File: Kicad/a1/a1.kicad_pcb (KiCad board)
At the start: 2 copper layers, 190 x 100 mm, 119 parts, among them J1 Conn_02x03_Odd_Even, J2 VGA, J3 AudioJack4, J4 Conn_02x17_Odd_Even, J6 Barrel Jack, J7 DE9_Plug, J8 DE9_Plug, SW1 Q, SW10 P, SW11 A, SW12 S, SW13 D, SW14 F, SW15 G, SW16 H, SW17 J, SW18 K, SW19 L, SW2 W, SW20 ENT, SW21 Z, SW22 X, SW23 C, SW24 V, SW25 SHIFT, SW26 ALT, SW27 B, SW28 N, SW29 M, SW3 E, SW30 SPACE, SW31 SW_Push, SW32 SW_SPDT, SW4 R, SW5 T, SW6 Y, SW7 U, SW8 I, SW9 O, U1 74HC590A, U10 74HC32, U11 74HC174, U12 74HC4520, U2 74HC590A, U3 62256, U4 SST39SF0x0, U5 W65C02SxP, U6 74HCT541, U7 74HC166, U8 74HC14, U9 74HC10, Y1 16Mhz

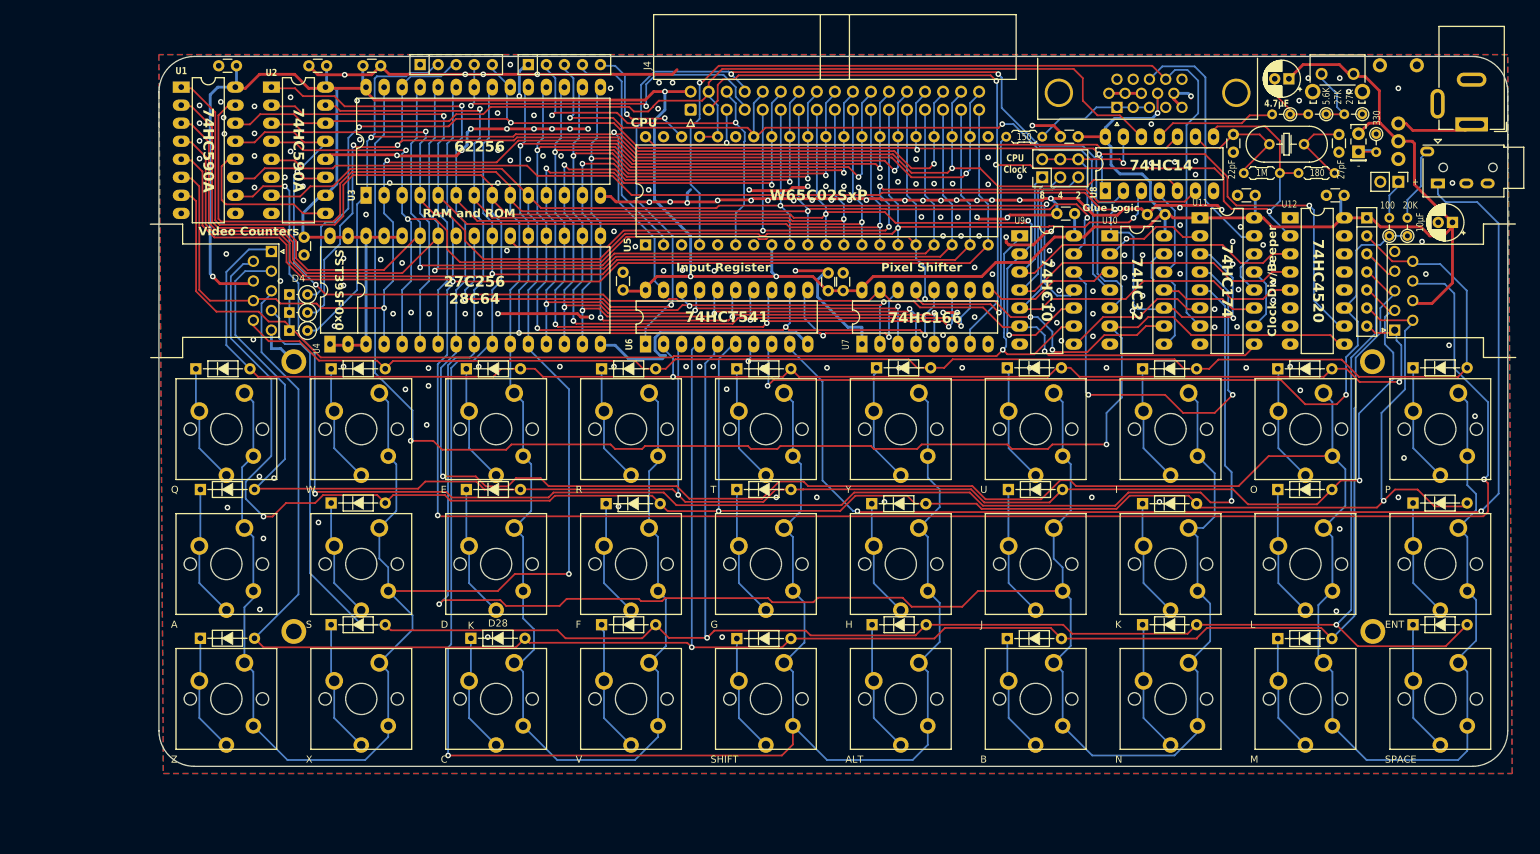
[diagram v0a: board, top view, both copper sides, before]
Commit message: tweak pcb, change key layout
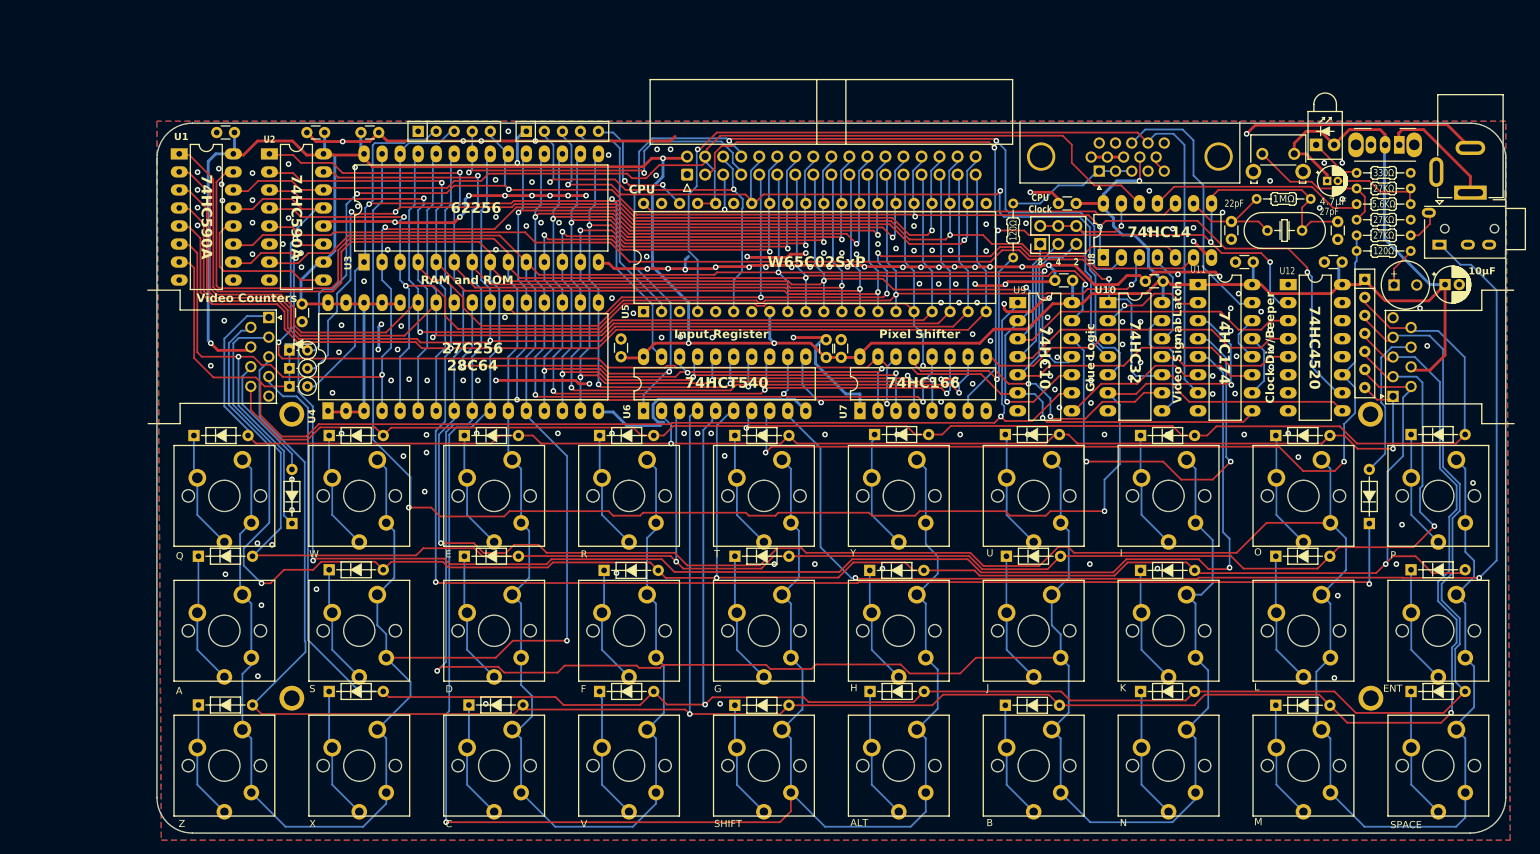
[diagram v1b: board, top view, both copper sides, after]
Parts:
- removed D1: LED, LED_THT:LED_Rectangular_W5.0mm_H2.0mm
- removed R11: 5.6K, PCM_Resistor_THT_US_AKL:R_Axial_DIN0204_L3.6mm_D1.6mm_P2.54mm_Vertical
- removed R12, R13: 27K, PCM_Resistor_THT_US_AKL:R_Axial_DIN0204_L3.6mm_D1.6mm_P2.54mm_Vertical
- removed R14: 20K, PCM_Resistor_THT_US_AKL:R_Axial_DIN0204_L3.6mm_D1.6mm_P2.54mm_Vertical
- added D37: LED, PCM_LED_THT_AKL:LED_Indicator_D3.0mm_W4.6mm_L6.5mm, F.Cu at (218.3, 43.1)
- added D5: 1N4148, PCM_Diode_THT_AKL_Double:D_DO-35_SOD27_P7.62mm_Horizontal, F.Cu at (225.8, 96.4)
- added D6: 1N4148, PCM_Diode_THT_AKL_Double:D_DO-35_SOD27_P7.62mm_Horizontal, F.Cu at (74.0, 96.4)
- added R6: 27KΩ, PCM_Resistor_THT_AKL_Double:R_Axial_DIN0204_L3.6mm_D1.6mm_P7.62mm_Horizontal, F.Cu at (224.0, 55.8)
- added R7: 120Ω, PCM_Resistor_THT_AKL_Double:R_Axial_DIN0204_L3.6mm_D1.6mm_P7.62mm_Horizontal, F.Cu at (175.6, 58.9)
- added R8: 120Ω, PCM_Resistor_THT_AKL_Double:R_Axial_DIN0204_L3.6mm_D1.6mm_P7.62mm_Horizontal, F.Cu at (224.0, 58.0)
- BZ1: footprint Connector_PinHeader_2.54mm:PinHeader_1x02_P2.54mm_Vertical -> Buzzer_Beeper:MagneticBuzzer_Kingstate_KCG0601
- C3: footprint PCM_Capacitor_THT_AKL:CP_Radial_D5.0mm_P2.00mm -> PCM_Capacitor_THT_AKL:CP_Radial_D4.0mm_P1.50mm
- R1: value 1M -> 330Ω; footprint PCM_Resistor_THT_AKL_Double:R_Axial_DIN0204_L3.6mm_D1.6mm_P5.08mm_Horizontal -> PCM_Resistor_THT_AKL_Double:R_Axial_DIN0204_L3.6mm_D1.6mm_P7.62mm_Horizontal
- R2: value 180 -> 1MΩ; footprint PCM_Resistor_THT_AKL_Double:R_Axial_DIN0204_L3.6mm_D1.6mm_P5.08mm_Horizontal -> PCM_Resistor_THT_AKL_Double:R_Axial_DIN0204_L3.6mm_D1.6mm_P7.62mm_Horizontal
- R3: value 150 -> 27KΩ; footprint PCM_Resistor_THT_AKL_Double:R_Axial_DIN0204_L3.6mm_D1.6mm_P5.08mm_Horizontal -> PCM_Resistor_THT_AKL_Double:R_Axial_DIN0204_L3.6mm_D1.6mm_P7.62mm_Horizontal
- R4: value 330 -> 27KΩ; footprint PCM_Resistor_THT_US_AKL:R_Axial_DIN0204_L3.6mm_D1.6mm_P2.54mm_Vertical -> PCM_Resistor_THT_AKL_Double:R_Axial_DIN0204_L3.6mm_D1.6mm_P7.62mm_Horizontal
- R5: value 100 -> 5.6KΩ; footprint PCM_Resistor_THT_US_AKL:R_Axial_DIN0204_L3.6mm_D1.6mm_P2.54mm_Vertical -> PCM_Resistor_THT_AKL_Double:R_Axial_DIN0204_L3.6mm_D1.6mm_P7.62mm_Horizontal
- U6: value 74HCT541 -> 74HCT540
- moved R3 58.2 mm to (231.6, 53.6), turned to 180 degrees
- moved R1 23.5 mm to (231.6, 47.0), turned to 180 degrees
- moved C3 15.4 mm to (219.8, 48.1), turned to 0 degrees
- moved BZ1 14.6 mm to (229.3, 62.8), turned to 0 degrees
- moved SW31 14.0 mm to (210.7, 44.3)
- moved C2 12.3 mm to (221.3, 53.9)
- moved C1 12.3 mm to (206.3, 53.9)
- moved Y1 12.2 mm to (211.4, 55.1)
- moved R2 11.6 mm to (209.9, 50.7), turned to 0 degrees
- moved J6 9.62 mm to (240.0, 49.8)
- moved C11 9.40 mm to (182.0, 51.3)
- moved C13 9.40 mm to (194.2, 62.3)
- moved C7 9.40 mm to (75.4, 68.0)
- moved C8 9.40 mm to (120.4, 70.4)
- moved D10 9.40 mm to (174.5, 83.9)
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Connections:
- C2 pad 1: Net-(C2-Pad1) -> /M16
- J7 pad 8: /A12 -> Net-(D6-A)
- J8 pad 8: /A11 -> Net-(D5-A)
- R1 pad 1: Net-(C1-Pad1) -> GND
- R1 pad 2: /M16 -> Net-(D37-K)
- R2 pad 1: Net-(C2-Pad1) -> Net-(C1-Pad1)
- R3 pad 1: Net-(U7-Qh) -> GND
- R3 pad 2: Net-(J2-Pad1) -> Net-(R3-Pad2)
- R4 pad 1: GND -> Net-(R3-Pad2)
- R4 pad 2: Net-(D1-Pad1) -> Net-(C3-Pad2)
- R5 pad 1: /BEEP -> Net-(C3-Pad2)
- R5 pad 2: /Speaker -> Net-(R5-Pad2)
- SW31 pad 1: Net-(R12-Pad1) -> Net-(R3-Pad2)
- U8 pad 11: Net-(R11-Pad2) -> Net-(R5-Pad2)
- Y1 pad 2: Net-(C2-Pad1) -> /M16
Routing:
- net /A11: track 397.2 -> 349.6 mm
- net GND: track 309.8 -> 341.3 mm, vias 205 -> 207
- net Net-(R5-Pad2): track 0.00 -> 30.2 mm
- net /A12: track 169.9 -> 197.2 mm, vias 3 -> 4
- net /HROW 2: track 310.4 -> 337.4 mm, vias 1 -> 2
- net Net-(D5-A): track 0.00 -> 21.7 mm
- net Net-(R3-Pad2): track 0.00 -> 20.8 mm
- net Net-(D6-A): track 0.00 -> 18.4 mm
- net Net-(R11-Pad2): track 16.5 -> 0.00 mm
- net Net-(C2-Pad1): track 11.8 -> 0.00 mm
- net /HROW 1: track 255.8 -> 267.1 mm
- net Net-(R12-Pad1): track 9.31 -> 0.00 mm
- net /V512: track 167.8 -> 175.7 mm
- net /HROW 3: track 314.8 -> 322.1 mm, vias 2 -> 1
- net Net-(D37-K): track 0.00 -> 7.29 mm
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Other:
- board text added: "MicroMicro v1 - Jan 2025"
- board text added: "Video Signal Latch"
- board text removed: "+"
- board text removed: "-"
- board text removed: "MicroMicro v1 - Dec 2024"

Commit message: Silkscreen tweaks
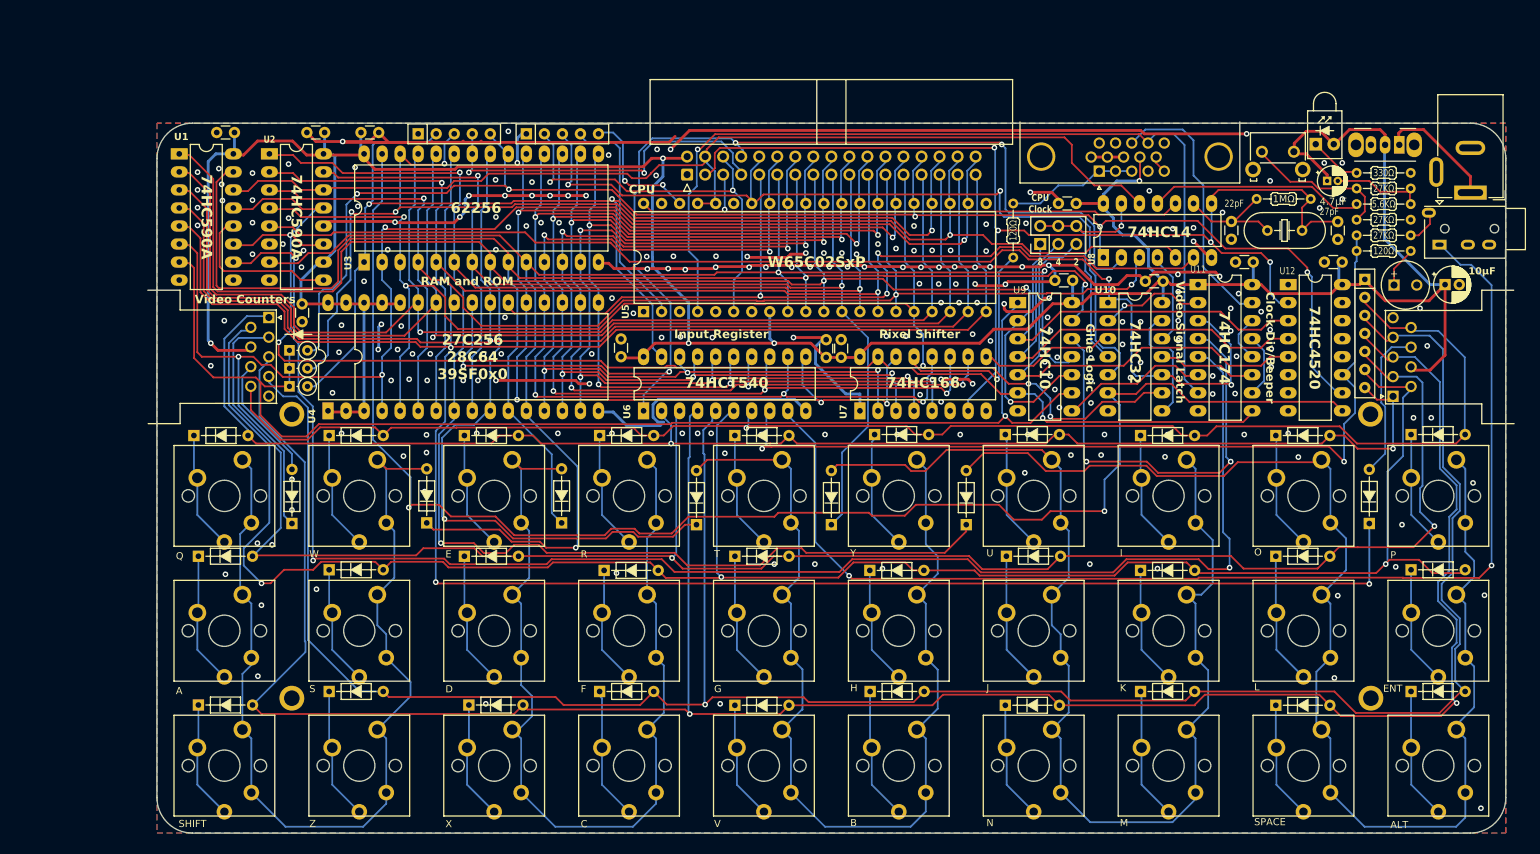
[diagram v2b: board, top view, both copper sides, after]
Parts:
- added D1: 1N4148, PCM_Diode_THT_AKL_Double:D_DO-35_SOD27_P7.62mm_Horizontal, F.Cu at (93.0, 96.3)
- added D38: 1N4148, PCM_Diode_THT_AKL_Double:D_DO-35_SOD27_P7.62mm_Horizontal, F.Cu at (112.0, 96.3)
- added D39: 1N4148, PCM_Diode_THT_AKL_Double:D_DO-35_SOD27_P7.62mm_Horizontal, F.Cu at (131.0, 96.6)
- added D40: 1N4148, PCM_Diode_THT_AKL_Double:D_DO-35_SOD27_P7.62mm_Horizontal, F.Cu at (150.0, 96.6)
- added D41: 1N4148, PCM_Diode_THT_AKL_Double:D_DO-35_SOD27_P7.62mm_Horizontal, F.Cu at (169.0, 96.6)
- SW21: value Z -> SHIFT
- SW22: value X -> Z
- SW23: value C -> X
- SW24: value V -> C
- SW25: value SHIFT -> V
- SW26: value ALT -> B
- SW27: value B -> N
- SW28: value N -> M
- SW29: value M -> SPACE
- SW30: value SPACE -> ALT
- moved RN2 0.35 mm to (107.0, 41.5)
- moved RN3 0.35 mm to (91.8, 41.5)
- moved SW31 0.30 mm to (210.7, 44.0)
- moved D37 0.11 mm to (218.2, 43.0)
- turned H2 to 180 degrees
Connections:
- SW1 pad 1: /A0 -> /COL 0
- SW10 pad 1: /A4 -> /COL 4
- SW11 pad 1: /A0 -> /COL 0
- SW12 pad 1: /A0 -> /COL 0
- SW13 pad 1: /A1 -> /COL 1
- SW14 pad 1: /A1 -> /COL 1
- SW15 pad 1: /A2 -> /COL 2
- SW16 pad 1: /A2 -> /COL 2
- SW17 pad 1: /A3 -> /COL 3
- SW18 pad 1: /A3 -> /COL 3
- SW19 pad 1: /A4 -> /COL 4
- SW2 pad 1: /A0 -> /COL 0
- SW20 pad 1: /A4 -> /COL 4
- SW21 pad 1: /A0 -> /COL 0
- SW22 pad 1: /A0 -> /COL 0
- SW23 pad 1: /A1 -> /COL 1
- SW24 pad 1: /A1 -> /COL 1
- SW25 pad 1: /A2 -> /COL 2
- SW26 pad 1: /A2 -> /COL 2
- SW27 pad 1: /A3 -> /COL 3
- SW28 pad 1: /A3 -> /COL 3
- SW29 pad 1: /A4 -> /COL 4
- SW3 pad 1: /A1 -> /COL 1
- SW30 pad 1: /A4 -> /COL 4
- SW4 pad 1: /A1 -> /COL 1
- SW5 pad 1: /A2 -> /COL 2
- SW6 pad 1: /A2 -> /COL 2
- SW7 pad 1: /A3 -> /COL 3
- SW8 pad 1: /A3 -> /COL 3
- SW9 pad 1: /A4 -> /COL 4
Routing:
- net /A3: track 387.9 -> 163.5 mm, vias 3 -> 2
- net /A2: track 458.6 -> 274.2 mm
- net /COL 4: track 0.00 -> 181.4 mm
- net /A4: track 421.2 -> 240.7 mm
- net /COL 3: track 0.00 -> 160.7 mm
- net /A0: track 359.1 -> 215.8 mm
- net /COL 2: track 0.00 -> 140.9 mm
- net /COL 1: track 0.00 -> 135.7 mm
- net /COL 0: track 0.00 -> 134.4 mm
- net /A1: track 331.1 -> 216.1 mm
- net GND: track 341.3 -> 415.4 mm, vias 207 -> 222
- net /~{WR}: track 205.4 -> 208.9 mm
- net /A13: track 174.9 -> 177.6 mm, vias 3 -> 4
- net /D4: track 150.8 -> 149.5 mm
- net /BEEP: track 123.6 -> 122.5 mm
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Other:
- board text added: "27C256 28C64 39SF0x0"
- board text added: "JLCJLCJLCJLC"
- board text removed: "27C256 28C64"

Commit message: Updated PCBs and Code
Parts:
- added C17: 100nF, PCM_Capacitor_THT_AKL_Double:C_Disc_D3.0mm_W1.6mm_P2.50mm, F.Cu at (240.8, 60.6)
- C1, C2: footprint Capacitor_THT:C_Disc_D3.0mm_W1.6mm_P2.50mm -> PCM_Capacitor_THT_AKL_Double:C_Disc_D3.0mm_W1.6mm_P2.50mm
- C10, C11, C12, C13, C14, C15, C4, C5, C6, C7, C8, C9: value C_Small -> 100nF; footprint Capacitor_THT:C_Disc_D3.0mm_W1.6mm_P2.50mm -> PCM_Capacitor_THT_AKL_Double:C_Disc_D3.0mm_W1.6mm_P2.50mm
- D37: value LED -> 1N4148; footprint PCM_LED_THT_AKL:LED_Indicator_D3.0mm_W4.6mm_L6.5mm -> PCM_Diode_THT_AKL_Double:D_DO-35_SOD27_P7.62mm_Horizontal
- D41: value 1N4148 -> LED; footprint PCM_Diode_THT_AKL_Double:D_DO-35_SOD27_P7.62mm_Horizontal -> PCM_LED_THT_AKL:LED_Indicator_D3.0mm_W4.6mm_L6.5mm
- moved D41 73.0 mm to (218.5, 42.9), turned to -90 degrees
- moved D37 72.7 mm to (169.0, 96.5), turned to 90 degrees
- moved C16 0.25 mm to (236.2, 62.7)
- moved R8 0.17 mm to (224.0, 58.2)
- moved C15 0.10 mm to (219.3, 59.6)
- moved R6 0.09 mm to (224.0, 55.9)
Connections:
- D37 pad 1: Net-(D37-K) -> /A4
- D37 pad 2: VCC -> /COL 4
- D41 pad 1: /A4 -> Net-(D41-K)
- D41 pad 2: /COL 4 -> VCC
- R1 pad 2: Net-(D37-K) -> Net-(D41-K)
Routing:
- net GND: track 415.4 -> 443.8 mm, vias 222 -> 225
- net /DataOut: track 5.28 -> 18.1 mm
- net Net-(D37-K): track 7.29 -> 0.00 mm
- net Net-(D41-K): track 0.00 -> 7.17 mm
- net VCC: track 447.0 -> 442.8 mm
- net /COL 1: track 135.7 -> 132.2 mm
- net /D7: track 168.6 -> 165.2 mm
- net /A9: track 175.4 -> 172.8 mm
- net /HROW 0: track 206.8 -> 204.5 mm
- net /HROW 3: track 322.1 -> 319.8 mm
- net /HROW 4: track 279.0 -> 276.8 mm
- net /HROW 1: track 266.9 -> 264.7 mm
- net /RAMHIDE: track 52.0 -> 50.5 mm
- net /COL 4: track 181.4 -> 179.9 mm
- net Net-(D9-K): track 17.7 -> 16.3 mm
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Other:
- board text added: "27C256 28C64B 39SF0x0"
- board text removed: "27C256 28C64 39SF0x0"

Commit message: tweak clock circuit
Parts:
- moved C1 19.1 mm to (187.6, 50.2)
- moved C10 19.1 mm to (130.5, 66.8)
- moved C11 19.1 mm to (163.2, 47.6)
- moved C12 19.1 mm to (162.7, 58.5)
- moved C14 19.1 mm to (188.2, 55.9)
- moved C2 19.1 mm to (202.6, 50.2)
- moved C3 19.1 mm to (201.1, 44.5)
- moved C8 19.1 mm to (101.6, 66.7)
- moved C9 19.1 mm to (132.6, 69.3)
- moved D12 19.1 mm to (212.9, 80.2)
- moved D13 19.1 mm to (174.8, 80.3)
- moved D14 19.1 mm to (137.3, 80.2)
- moved D15 19.1 mm to (98.6, 80.3)
- moved D18 19.1 mm to (79.5, 97.3)
- moved D20 19.1 mm to (155.9, 97.3)
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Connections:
- C2 pad 1: /M16 -> Net-(U12A-Enable)
- R2 pad 2: /M16 -> Net-(U12A-Enable)
- U12 pad 2: /M16 -> Net-(U12A-Enable)
- U12 pad 3: /M8 -> /M16
- U12 pad 4: /M4 -> /M8
- U12 pad 5: /M2 -> /M4
- U12 pad 6: unconnected-(U12A-Q4-Pad6) -> /M2
- U8 pad 8: /M16 -> Net-(U12A-Enable)
- Y1 pad 2: /M16 -> Net-(U12A-Enable)
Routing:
- net Net-(U12A-Enable): track 0.00 -> 36.6 mm
- net /M16: track 161.0 -> 132.9 mm, vias 4 -> 3
- net /A15: track 206.7 -> 208.8 mm
